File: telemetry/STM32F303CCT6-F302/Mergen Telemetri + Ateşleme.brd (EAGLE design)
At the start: 49.7 x 87.2 mm, 90 parts, among them J2 U.FL, Q2 IRLML6344TRPBF, Q3 IRLML6344TRPBF, U2 BMP280, U3 MPU-6050, U4 L86, U6 AMS1117-3.3, U7 AMS1117-3.3, Y2 ABM3B-26.000MHZ-10-1-U-T

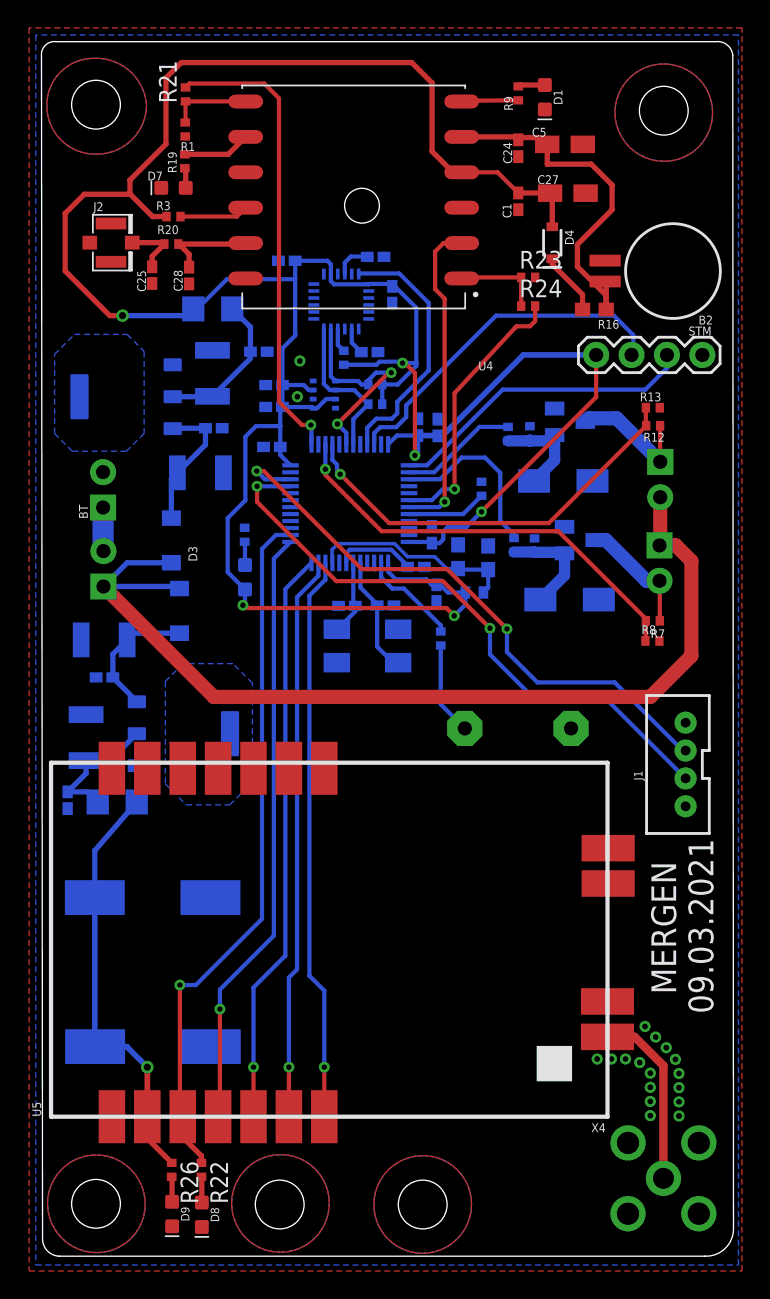
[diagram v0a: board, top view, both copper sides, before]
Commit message: New version of boards with new controller was designed
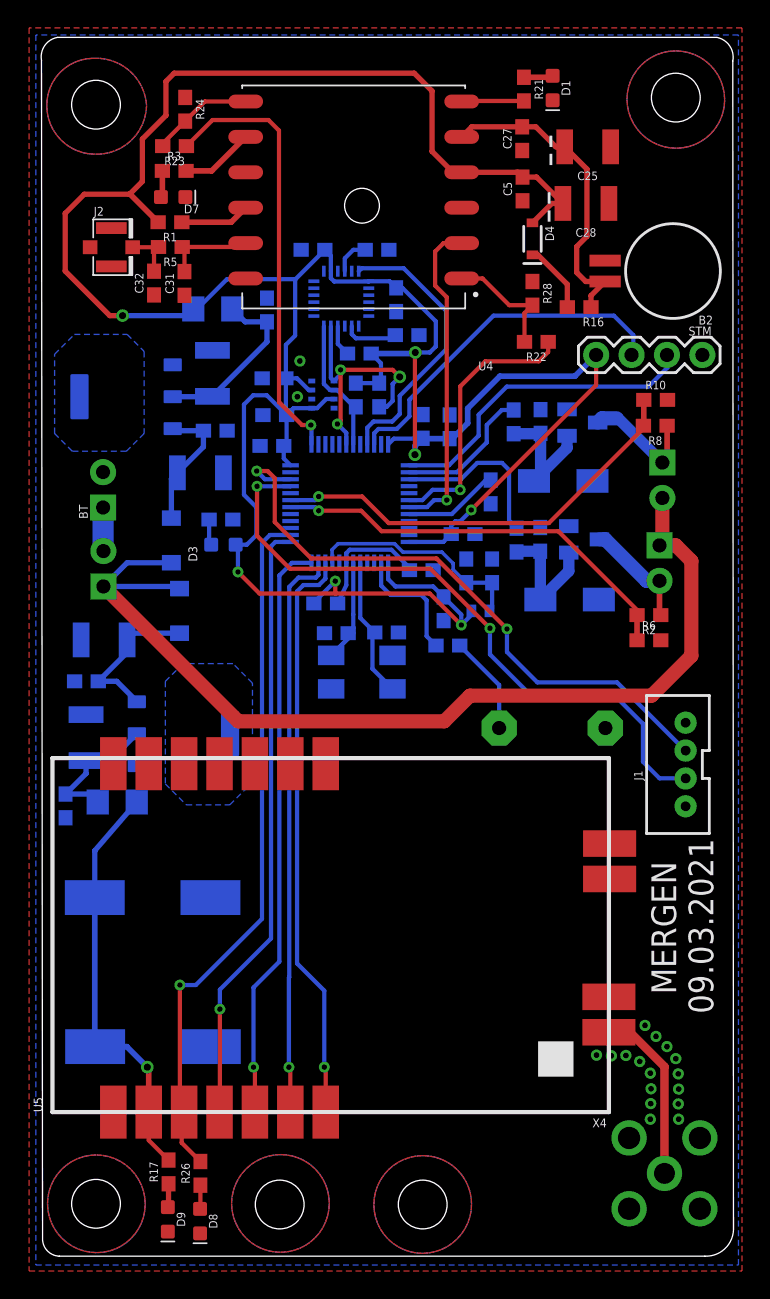
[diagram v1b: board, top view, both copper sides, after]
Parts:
- removed C1, C24: 100nF, rcl:C0402K
- removed C33, C34: 0.1uF, rcl:C0402K
- removed C35: 4.7uF, rcl:C0402K
- removed R12: 10k, rcl:R0402
- removed R13: 3k3, rcl:R0402
- removed R14: 20, rcl:R0402
- removed R15: 4.7K, rcl:R0402
- added C10: 4.7uF, SparkFun-Capacitors:0603
- added C19: 25pF, SparkFun-Capacitors:0603
- added C20: 2.2nF, SparkFun-Capacitors:0603
- added C21, C22: 0.1uF, SparkFun-Capacitors:0603
- added R18, R29: 4k7, SparkFun-Resistors:0603
- added R27: 1k, SparkFun-Resistors:0603
- added R28: 10k, SparkFun-Resistors:0603
- added R30: 20, SparkFun-Resistors:0603
- C11, C12, C13: value 0.1uF -> 100nF; device rcl:C0402K -> SparkFun-Capacitors:0603
- C14, C18, C23, C3, C31, C32, C4, C8, C9: device rcl:C0402K -> SparkFun-Capacitors:0603
- C15: value 15pF -> 25pF; device rcl:C0402K -> SparkFun-Capacitors:0603
- C16: value 15pF -> 100nF; device rcl:C0402K -> SparkFun-Capacitors:0603
- C25: value 0.1uF -> 4.7uF; device rcl:C0402K -> SparkFun-Capacitors:EIA3528
- C27: value 10uF -> 100nF; device rcl:R/2012-12W -> SparkFun-Capacitors:0603
- C28: value 0.1uF -> 10uF; device rcl:C0402K -> SparkFun-Capacitors:EIA3528
- C30: value 2.2nF -> 0.1uF; device rcl:C0402K -> SparkFun-Capacitors:0603
- C5: value 4.7uF -> 100nF; device rcl:R/2012-12W -> SparkFun-Capacitors:0603
- R1, R2: device rcl:R0402 -> SparkFun-Resistors:0603
- R10: value 20 -> 3k3; device rcl:R0402 -> SparkFun-Resistors:0603
- R11: value 220 -> 10k; device rcl:R0402 -> SparkFun-Resistors:0603
- R17: value 1k -> 1k5; device rcl:R0402 -> SparkFun-Resistors:0603
- R19: value 100 -> 4k7; device rcl:R0402 -> SparkFun-Resistors:0603
- R20: value 0R -> 4k7; device rcl:R0402 -> SparkFun-Resistors:0603
- R21: value 680 -> 470; device rcl:R0402 -> SparkFun-Resistors:0603
- R22: value 3K3 -> 680; device rcl:R0402 -> SparkFun-Resistors:0603
- R23: value 10k -> 680; device rcl:R0402 -> SparkFun-Resistors:0603
- R24: value 680 -> 10k; device rcl:R0402 -> SparkFun-Resistors:0603
- R25: value 4.7K -> 10k; device rcl:R0402 -> SparkFun-Resistors:0603
- R26: value 1k5 -> 3k3; device rcl:R0402 -> SparkFun-Resistors:0603
- R3: value 10k -> 100; device rcl:R0402 -> SparkFun-Resistors:0603
- R4: value 4.7K -> 20; device rcl:R0402 -> SparkFun-Resistors:0603
- R5: value 4.7K -> 0; device rcl:R0402 -> SparkFun-Resistors:0603
- R6: value 4.7K -> 3k3; device rcl:R0402 -> SparkFun-Resistors:0603
- R7: value 10k -> 220; device rcl:R0402 -> SparkFun-Resistors:0603
- R8: value 3k3 -> 10k; device rcl:R0402 -> SparkFun-Resistors:0603
- R9: value 470 -> 4k7; device rcl:R0402 -> SparkFun-Resistors:0603
- moved R22 64.1 mm to (70.0, 43.6), turned to 180 degrees
- moved R17 46.0 mm to (43.6, -16.0), flipped to the top
- moved R20 33.9 mm to (70.3, 29.4), flipped to the bottom, turned to 90 degrees
- moved C25 32.6 mm to (73.7, 57.6), turned to 180 degrees
- moved C28 28.9 mm to (73.6, 53.5), turned to 180 degrees
- moved R24 28.4 mm to (44.8, 60.3), turned to 270 degrees
- moved R23 27.1 mm to (44.1, 57.7), turned to 180 degrees
- moved R6 25.9 mm to (78.1, 22.2), flipped to the top
- moved C16 25.6 mm to (58.6, 50.2)
- moved R21 24.3 mm to (69.1, 61.7), turned to 270 degrees
- moved C18 22.7 mm to (61.8, 27.2), turned to 0 degrees
- moved R9 21.9 mm to (57.3, 42.8), flipped to the bottom, turned to 180 degrees
- moved R19 21.8 mm to (58.8, 39.8), flipped to the bottom
- moved C31 19.7 mm to (44.8, 47.8), flipped to the top
- moved R5 17.7 mm to (43.8, 50.4), flipped to the top, turned to 180 degrees
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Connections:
- net 3.3V: now also C10.2, C11.2, C12.2, C13.2, C14.2, C21.2, C22.2, C23.2, C28.A, C30.2, C5.2, R1.2, R11.1, R18.2, R19.2, R9.2; no longer C1.1, C11.1, C12.1, C13.1, C14.1, C27.+, C31.1, C32.1, C33.1, C34.1, C35.1, R25.1, R3.2, R5.1, R6.1
- net 5V: now also R17.2; no longer R26.1
- net APG: now also R8.1; no longer R12.1
- net APG_F: now also R30.1; no longer R14.1
- net APG_S: now also R10.1, R8.2, U1.19; no longer R12.2, R13.1, U1.28
- net AUX: now also R26.2; no longer R22.1
- net BT0: now also R25.1; no longer R2.1
- net BZZR: now also R7.2; no longer R11.1
- net FN: now also R23.1; no longer R21.2
- net GND: now also C10.1, C11.1, C12.1, C13.1, C14.1, C16.1, C18.1, C19.2, C20.1, C21.1, C22.1, C23.1, C25.C, C27.1, C28.C, C30.1, C31.1, C32.1, C5.1, R10.2, R20.2, R24.1, R25.2, R27.2, R28.1, R29.2, R6.2; no longer C1.2, C11.2, C12.2, C13.2, C14.2, C16.2, C18.2, C23.2, C24.2, C25.2, C27.-, C28.2, C30.2, C31.2, C32.2, C33.2, C34.2, C35.2, C5.-, R1.2, R13.2, R15.1, R17.2, R2.2, R23.2, R4.1, R8.2
- net MAIN: now also R2.1; no longer R7.1
- net MAIN_F: now also R4.1; no longer R10.1
- net MAIN_S: now also R2.2, R6.1, U1.18; no longer R7.2, R8.1, U1.27
- net N$10: now also R21.2; no longer R9.2
- net N$11: now also R21.1; no longer R9.1
- net N$13: now also R20.1; no longer R10.2
- net N$14: now also R17.1; no longer R26.2
- net N$15: now also R27.1; no longer R17.1
- net N$16: now also R3.2; no longer R19.2
- net N$17: now also R3.1; no longer R19.1
- net N$18: now also C16.2; no longer C18.1
- net N$19: now also C32.2, R5.2; no longer C25.1, R20.1
- net N$20: now also R23.2, R24.2; no longer R1.1, R21.1
- net N$21: now also R26.1; no longer R22.2
- net N$22: now also C20.2; no longer C30.1
- net N$3: now also R1.1; no longer R3.1
- net N$6: now also R29.1, R30.2; no longer R14.2, R15.2
- net N$8: now also R7.1; no longer R11.2
- net NRST: now also C18.2, R11.2; no longer C23.1
- net OSC_IN: now also C19.1; no longer C15.1
- net OSC_OUT: now also C15.1; no longer C16.1
- net PIN22: now also R9.1; no longer R25.2
- net SCL: now also R19.1; no longer R5.2
- net SDA: now also R18.1; no longer R6.2
- net TX1: now also R22.1; no longer R24.2
- net TXD: now also R22.2, R28.2; no longer R23.1, R24.1
- net V_BCKP: now also C25.A, C27.2; no longer C24.1, C5.+
- net XANT: now also C31.2, R5.1; no longer C28.1, R20.2
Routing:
- net 3.3V: track 213.1 -> 218.3 mm, vias 6 -> 7
- net OSC_OUT: track 5.40 -> 9.91 mm
- net NRST: track 5.76 -> 9.10 mm
- net V_BCKP: track 26.1 -> 22.8 mm
- net TX3: track 43.6 -> 46.6 mm
- net SCL: track 15.6 -> 18.3 mm, vias 2 -> 3
- net TXD: track 6.36 -> 8.74 mm
- net N$6: track 7.46 -> 9.78 mm
- net N$22: track 1.94 -> 3.92 mm
- net N$5: track 10.8 -> 12.7 mm
- net RX3: track 42.7 -> 44.6 mm
- net FN: track 33.4 -> 31.6 mm
- net INT: track 18.5 -> 20.3 mm
- net N$13: track 7.70 -> 9.41 mm
- net BZZR: track 7.19 -> 8.86 mm
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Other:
- board size 49.7 x 87.2 mm -> 49.7 x 87.5 mm

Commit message: Connector was changed and Preparing first order
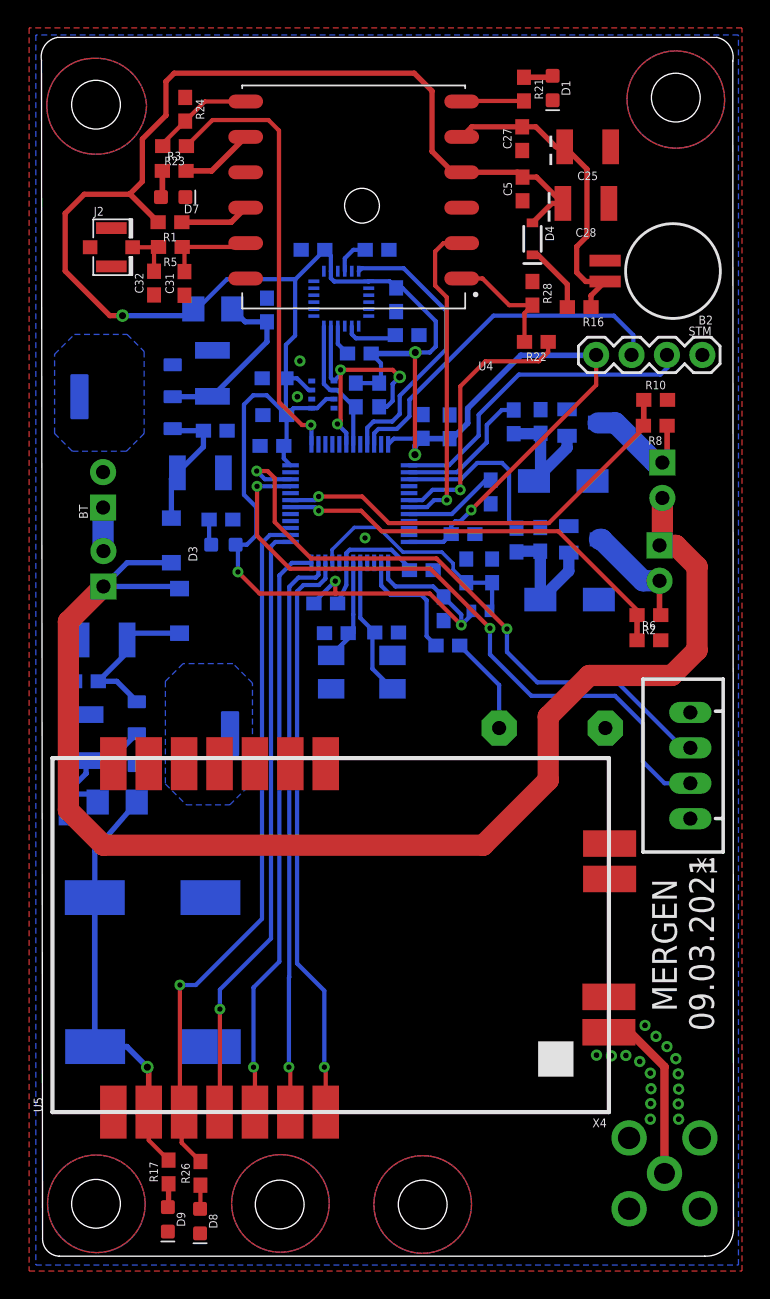
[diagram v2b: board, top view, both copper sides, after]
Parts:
- removed J1: (no value), SparkFun-Connectors:JST-4-PTH-VERT
- added X1: JST-XH-04-PIN-LONG-PAD, Rembrandt Electronics - JST XH Connectors v1-0:JST-XH-04-PACKAGE-LONG-PAD
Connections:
- net GND: now also X1.1, X1.4; no longer J1.1, J1.4
- net RX3: now also X1.3; no longer J1.3
- net TX3: now also X1.2; no longer J1.2
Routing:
- net VCC: track 72.3 -> 95.6 mm
- net VDDA: track 16.1 -> 17.1 mm
